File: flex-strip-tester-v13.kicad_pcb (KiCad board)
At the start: 2 copper layers, 68.8 x 11.1 mm, 15 parts, among them J2 Conn_01x01_Female

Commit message: osh park freebie version to fab
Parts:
- removed the D1 at (153.2, 96.0)
- removed the Ref** at (169.8, 117.8)
- removed the Ref** at (154.3, 117.8)
- added REF**: d, digikey-footprints:Diode_DO-35_P10mm, F.Cu at (153.2, 94.0)
- added Ref**: Val**, flextester:oshpark-v2-osh, F.Cu at (118.4, 92.5)
- added Ref**: Val**, flextester:oshpark-v2-osh, F.Cu at (147.7, 81.3)
- added Ref**: Val**, flextester:oshpark-v2-osh, F.Cu at (167.2, 118.1)
- added Ref**: Val**, flextester:oshpark-v2-osh, F.Cu at (151.8, 118.1)
- added Ref**: Val**, flextester:oshpark-v2-osh, F.Cu at (110.0, 77.0)
- REF**: value R_0603 -> R_0603_1608Metric; moved to F.Cu
- moved REF** 15.4 mm to (158.8, 95.6), turned to 90 degrees
- moved J2 3.15 mm to (184.4, 96.5) (x4)
- moved J2 2.98 mm to (122.2, 96.5) (x4)
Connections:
- D1 pad 1: GND -> +3V3
- D1 pad 2: +3V3 -> GND
- REF** pad 2: GND -> (no net)
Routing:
- net (no net): track 0.00 -> 4.98 mm, vias 0 -> 1
- net +3V3: track 30.2 -> 34.7 mm
- net GND: track 37.6 -> 39.4 mm, vias 3 -> 1
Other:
- board size 68.8 x 11.1 mm -> 74.4 x 11.1 mm
- board text added: "-"
- board text added: "R"
- board text added: "oshpark.com/ flex"
- board text removed: "github.com/ oshpark/ flextester"

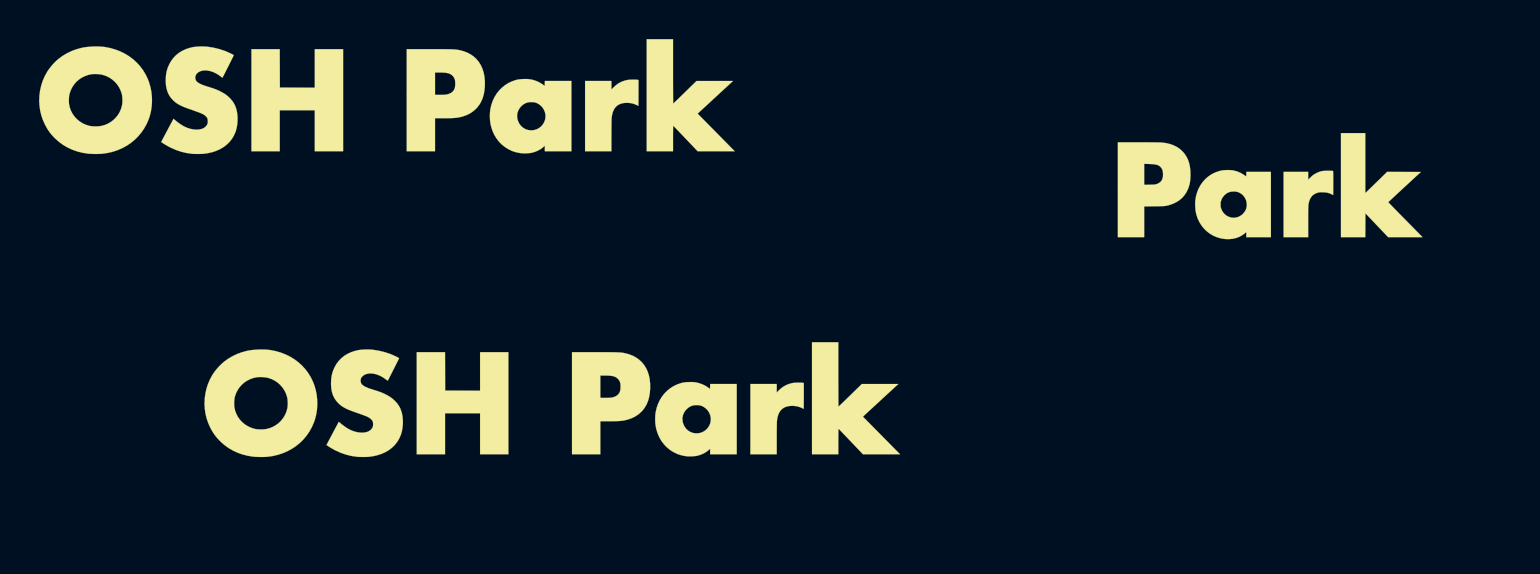
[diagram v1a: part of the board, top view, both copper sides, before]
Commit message: update silkscreen layer names for plot
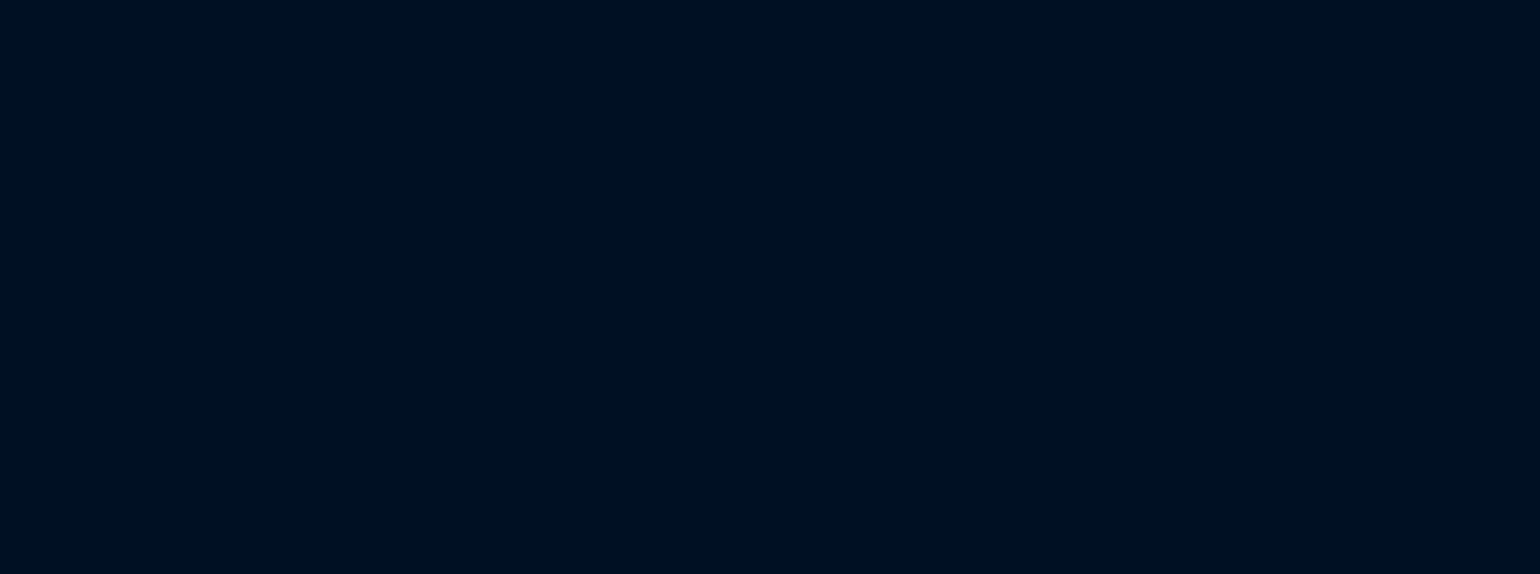
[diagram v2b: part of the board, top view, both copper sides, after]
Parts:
- removed the Ref** at (118.4, 92.5)
- removed the Ref** at (147.7, 81.3)
- removed the Ref** at (110.0, 77.0)
